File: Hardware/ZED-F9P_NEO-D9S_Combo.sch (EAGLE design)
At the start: 97 parts, among them J1 ANTENNA-SMA-GROUNDEDEDGE_SMA, J2 Qwiic Right Angle, J3 USB Female Type C Connector, J4 Qwiic Right Angle, J6 USB Female Type C Connector, U1 U-BLOX_NEO-D9S-00B, U2 3.3V, U3 POWER-DIVIDER, U4 U-BLOX_ZED-F9P

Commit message: Updates various text and symbols
* Replaces ESD Diodes and Antenna Splitter Diode with larger packages
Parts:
- removed D2, D4: PRTR5V0U2F, SparkFun-IC-Power:PRTR5V0U2F
- removed U$78: SPARKX-LOGO4, SparkX:SPARKX-LOGO4
- added LOGO2: SFE_LOGO_NAME.1_INCH, SparkFun-Aesthetics:SFE_LOGO_NAME.1_INCH
- added U5, U6: ESD Diode, SparkFun-DiscreteSemi:TVS_DIODE_ARRAY_DT1042-04SO-7
- LED1: device SparkFun-LED:LED-RED0603 -> SparkFun-LED:LED-RED_0603-KB
- R1: value 1k -> 4.7k; device SparkFun-Resistors:1KOHM-0603-1/10W-1% -> SparkFun-Resistors:4.7KOHM-0603-1/10W-1%
- U$77: value SPARKX-LOGO4 -> BP2G1+_POWER_SPLITTER; device SparkX:SPARKX-LOGO4 -> SparkFun-RF:BP2G1+_POWER_SPLITTER
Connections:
- net ANT: now also U$77.S
- net ANT_NEO: now also U$77.1
- net ANT_ZED: now also U$77.2
- net D+_NEO: now also U5.IO4; no longer D4.6
- net D+_ZED: now also U6.IO4; no longer D2.6
- net D-_NEO: now also U5.IO3; no longer D4.4
- net D-_ZED: now also U6.IO3; no longer D2.4
- net GND: now also U$77.GND, U5.VSS, U6.VSS; no longer D2.2, D4.2
- net USB_D+: now also U6.IO1; no longer D2.1
- net USB_D+1: now also U5.IO1; no longer D4.1
- net USB_D-: now also U6.IO2; no longer D2.3
- net USB_D-1: now also U5.IO2; no longer D4.3
- net V_USB: now also U6.VCC; no longer D2.5
- net V_USB_2: now also U5.VCC; no longer D4.5
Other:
- note added: "Antenna Divider - BP2G1+"
- note added: "GNSS Module: u-blox ZED-F9P"
- note added: "Iout (max): 600mA Vin (max): 6.5V Vdrop (max): 250mV Iq: 55uA"
- note added: "L-Band Corrections Module: u-blox NEO-D9S"
- note added: "L1/L2 Antenna"
- note added: "Revised By: Elias Santistevan"
- note added: "Voltage Regulation - AP2112K"
- note added: "v10"
- note removed: "AP2112K-3.3V ------------- Iout (max): 600mA Vin (max): 6.5V Vdrop (max): 250mV Iq: 55uA"
- note removed: "Antenna"
- note removed: "Antenna Divider"
- note removed: "Voltage Regulation"
- note removed: "u-blox NEO-D9S"
- note removed: "u-blox ZED-F9P"
- note removed: "x02"
- moved on the sheet: C3, I2C, R7, R8, RX2-TX2, TX2-RX2, U3

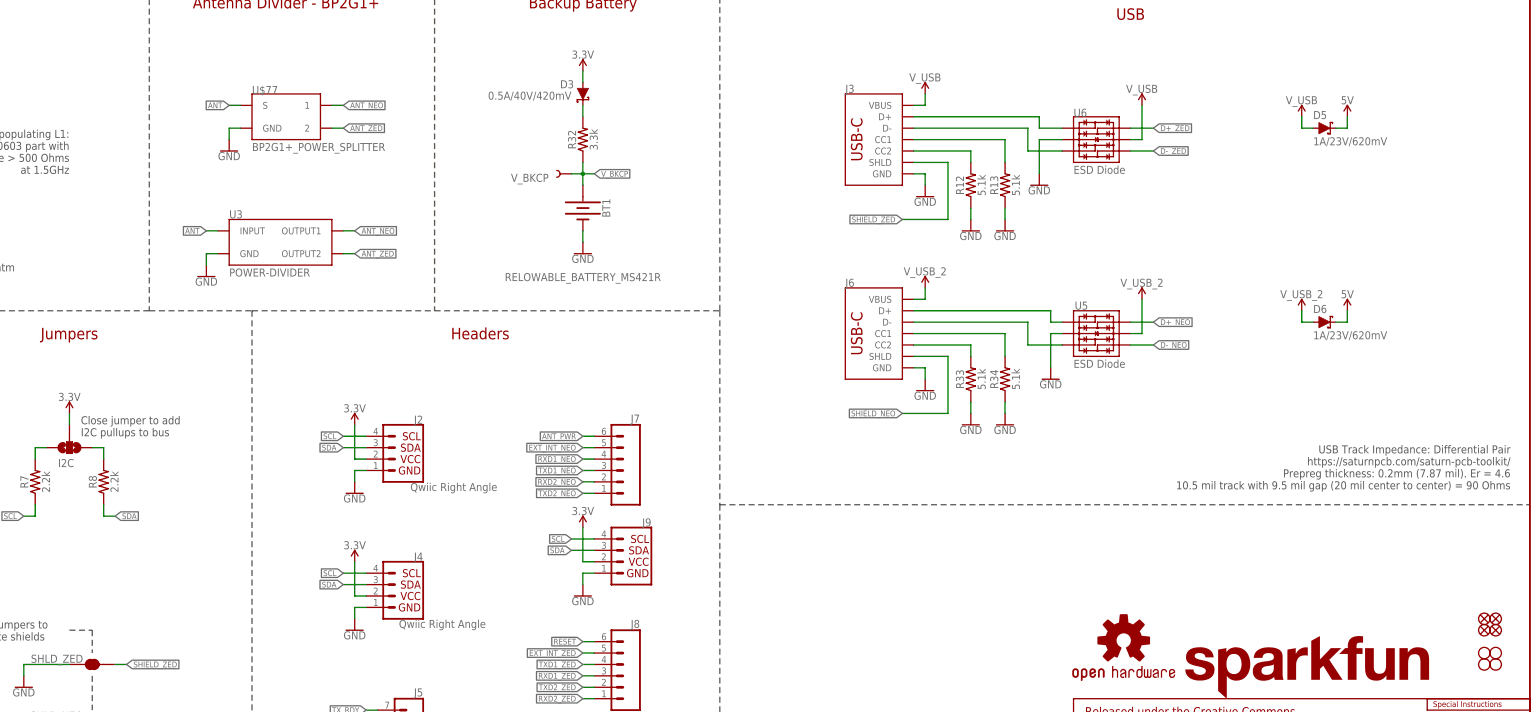
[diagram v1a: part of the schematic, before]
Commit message: Changes 90 Ohm impedance calculation to decrease trace width
* Adds additional measures
* Updates silk
* Adds polygons to USB shield
* Adds four layer numbers
* Updated ordering instructions
* Routes new antenna splitter
* Spaces out some of the more common transmission traces, UART and I2C, to minimize cross talk
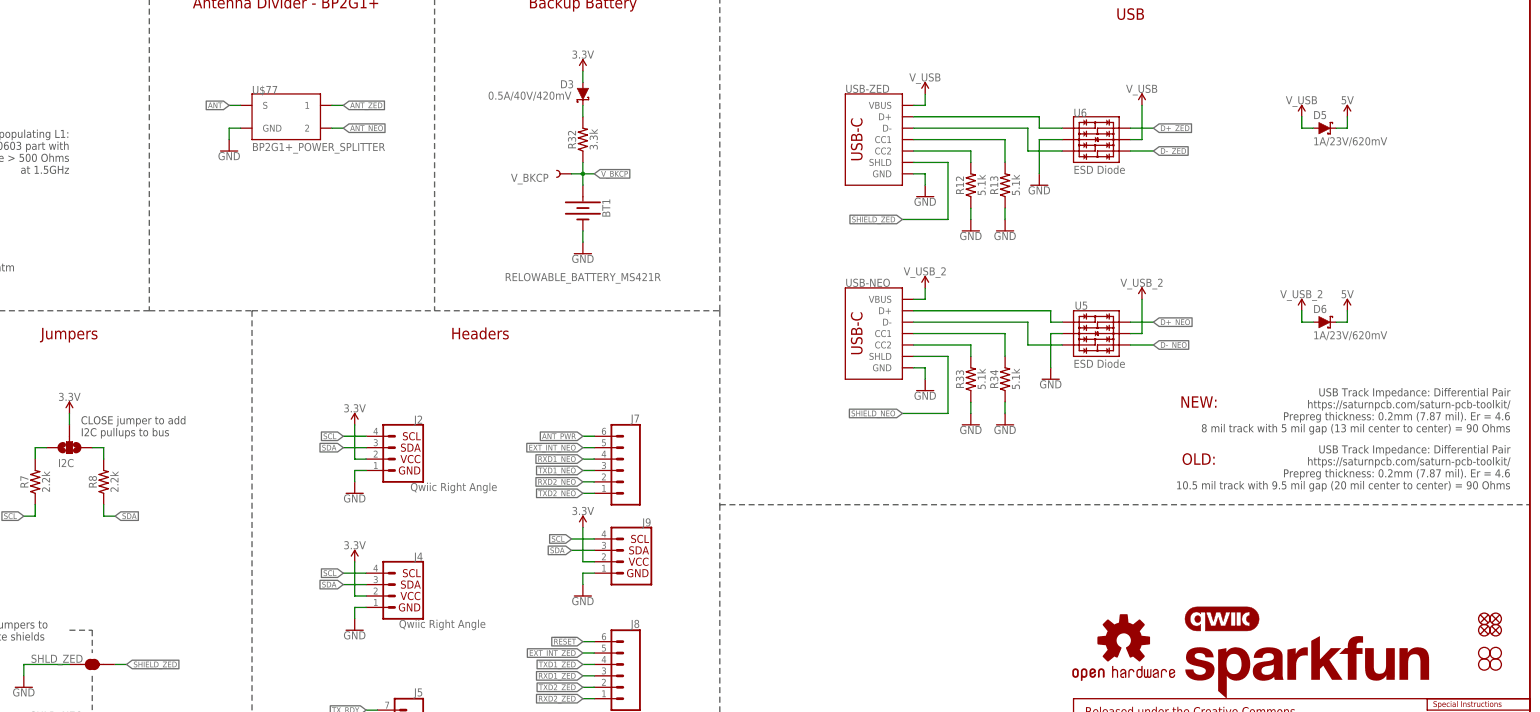
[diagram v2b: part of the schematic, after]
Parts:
- removed U3: POWER-DIVIDER, SparkFun-RF:POWER-DIVIDER
- added LOGO3: QWIIC_LOGO_5MM, SparkFun-Aesthetics:QWIIC_LOGO_5MM
- renumbered J3 to USB-ZED, J6 to USB-NEO
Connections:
- net ANT: no longer U3.INPUT
- net ANT_NEO: now also U$77.2; no longer U$77.1, U3.OUTPUT1
- net ANT_ZED: now also U$77.1; no longer U$77.2, U3.OUTPUT2
- net GND: no longer U3.GND
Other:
- note added: "CLOSE jumper to add I2C pullups to bus"
- note added: "NEW:"
- note added: "OLD:"
- note added: "USB Track Impedance: Differential Pair https://saturnpcb.com/saturn-pcb-toolkit/ Prepreg thickness: 0.2mm (7.87 mil). Er = 4.6 8 mil track with 5 mil gap (13 mil center to center) = 90 Ohms"
- note removed: "Close jumper to add I2C pullups to bus"

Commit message: Fixes ESD diode
* Adds L-Band text/silk to relevant Antenna notes
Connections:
- removed net USB_D+: U6.IO1, USB-ZED.D+
- removed net USB_D+1: U5.IO1, USB-NEO.D+
- removed net USB_D-: U6.IO2, USB-ZED.D-
- removed net USB_D-1: U5.IO2, USB-NEO.D-
- net D+_NEO: now also USB-NEO.D+
- net D+_ZED: now also USB-ZED.D+
- net D-_NEO: now also USB-NEO.D-
- net D-_ZED: now also USB-ZED.D-
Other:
- note added: "L1/L2/L-Band Antenna"
- note removed: "L1/L2 Antenna"
- note removed: "NEW:"
- note removed: "OLD:"
- note removed: "USB Track Impedance: Differential Pair https://saturnpcb.com/saturn-pcb-toolkit/ Prepreg thickness: 0.2mm (7.87 mil). Er = 4.6 10.5 mil track with 9.5 mil gap (20 mil center to center) = 90 Ohms"
- moved on the sheet: U5, U6

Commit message: Updates note for USB 90 Ohm impedance calculation
* Moves all silk out towards the PTH's
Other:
- note added: "USB Track Impedance: Differential Pair https://saturnpcb.com/saturn-pcb-toolkit/ Prepreg thickness: 0.2mm (7.1 mil). Er = 4.6 8 mil track with 5 mil gap (13 mil center to center) = 90 Ohms"
- note removed: "USB Track Impedance: Differential Pair https://saturnpcb.com/saturn-pcb-toolkit/ Prepreg thickness: 0.2mm (7.87 mil). Er = 4.6 8 mil track with 5 mil gap (13 mil center to center) = 90 Ohms"
- moved on the sheet: J1
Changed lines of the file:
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@@
 <text x="427.482" y="91.948" size="1.778" layer="97" font="vector" align="top-right">USB Track Impedance: Differential Pair
 https://saturnpcb.com/saturn-pcb-toolkit/
-Prepreg thickness: 0.2mm (7.87 mil). Er = 4.6
+Prepreg thickness: 0.2mm (7.1 mil). Er = 4.6
 8 mil track with 5 mil gap (13 mil center to center) = 90 Ohms
 </text>
@@
 <attribute name="VALUE" x="217.932" y="233.934" size="1.778" layer="96" font="vector" rot="R180" align="top-center"/>
 </instance>
-<instance part="J1" gate="G$1" x="35.56" y="175.26" smashed="yes" rot="MR0">
-<attribute name="NAME" x="40.132" y="176.53" size="1.778" layer="95" font="vector" rot="MR0"/>
+<instance part="J1" gate="G$1" x="35.56" y="177.8" smashed="yes" rot="MR0">
+<attribute name="NAME" x="40.132" y="179.07" size="1.778" layer="95" font="vector" rot="MR0"/>
 </instance>
 <instance part="J5" gate="J1" x="180.34" y="22.86" smashed="yes" rot="MR0">
@@
 </instance>
 <instance part="C7" gate="G$1" x="73.66" y="172.72" smashed="yes" rot="R90">
-<attribute name="NAME" x="70.739" y="174.244" size="1.778" layer="95" font="vector" rot="R90"/>
-<attribute name="VALUE" x="75.819" y="174.244" size="1.778" layer="96" font="vector" rot="R90"/>
+<attribute name="NAME" x="72.136" y="179.959" size="1.778" layer="95" font="vector" rot="R180"/>
+<attribute name="VALUE" x="72.136" y="177.419" size="1.778" layer="96" font="vector" rot="R180"/>
 </instance>
 <instance part="FRAME2" gate="G$1" x="0" y="0" smashed="yes"/>
@@
 <pinref part="J1" gate="G$1" pin="GND"/>
 <pinref part="GND27" gate="1" pin="GND"/>
-<wire x1="33.02" y1="172.72" x2="33.02" y2="170.18" width="0.1524" layer="91"/>
+<wire x1="33.02" y1="175.26" x2="33.02" y2="170.18" width="0.1524" layer="91"/>
 </segment>
 <segment>
@@
 <junction x="45.72" y="172.72"/>
 <pinref part="J1" gate="G$1" pin="SIGNAL"/>
+<wire x1="35.56" y1="175.26" x2="35.56" y2="172.72" width="0.1524" layer="91"/>
 <wire x1="35.56" y1="172.72" x2="45.72" y2="172.72" width="0.1524" layer="91"/>
 <pinref part="L1" gate="L1" pin="1"/>

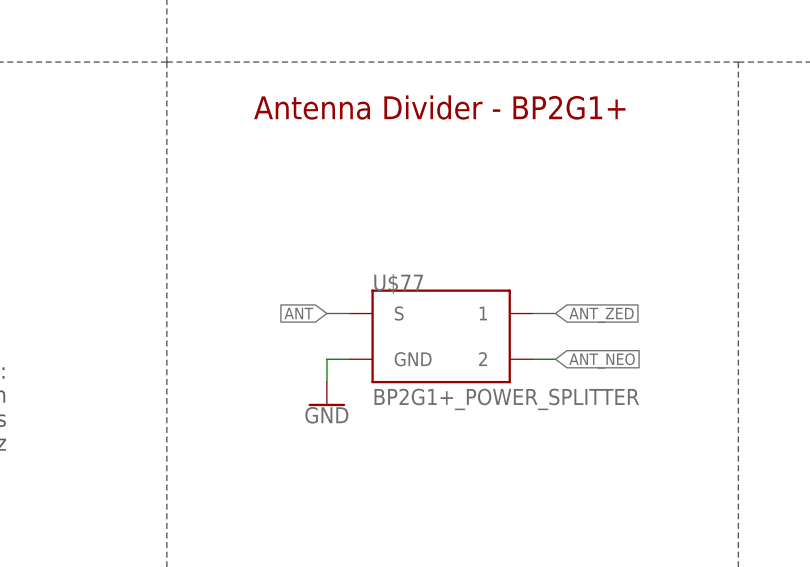
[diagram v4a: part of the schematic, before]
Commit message: Updates BP2G1+ with minor corrections
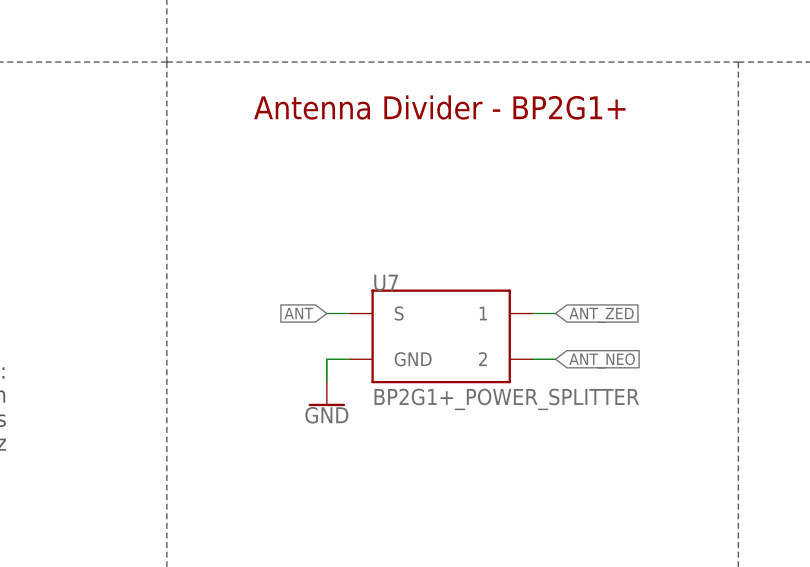
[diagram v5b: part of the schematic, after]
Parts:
- renumbered U$77 to U7
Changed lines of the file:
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@@
 <part name="U6" library="SparkFun-DiscreteSemi" deviceset="TVS_DIODE_ARRAY" device="_DT1042-04SO-7" value="ESD Diode"/>
 <part name="SUPPLY26" library="SparkFun-PowerSymbols" deviceset="V_USB_2" device=""/>
-<part name="U$77" library="SparkFun-RF" deviceset="BP2G1+_POWER_SPLITTER" device=""/>
+<part name="U7" library="SparkFun-RF" deviceset="BP2G1+_POWER_SPLITTER" device=""/>
 <part name="GND24" library="SparkFun-PowerSymbols" deviceset="GND" device=""/>
 <part name="LOGO3" library="SparkFun-Aesthetics" deviceset="QWIIC_LOGO" device="_5MM" value="QWIIC_LOGO_5MM"/>
@@
 <attribute name="VALUE" x="335.28" y="127.254" size="1.778" layer="96" font="vector" align="bottom-center"/>
 </instance>
-<instance part="U$77" gate="U1" x="154.94" y="165.1" smashed="yes">
-<attribute name="NAME" x="147.32" y="170.18" size="1.778" layer="95" font="vector"/>
-<attribute name="VALUE" x="147.32" y="157.48" size="1.778" layer="96" font="vector"/>
+<instance part="U7" gate="U1" x="154.94" y="165.1" smashed="yes">
+<attribute name="NAME" x="147.32" y="170.18" size="1.778" layer="95"/>
+<attribute name="VALUE" x="147.32" y="157.48" size="1.778" layer="96"/>
 </instance>
 <instance part="GND24" gate="1" x="142.24" y="157.48" smashed="yes">
@@
 <pinref part="GND24" gate="1" pin="GND"/>
 <wire x1="142.24" y1="162.56" x2="142.24" y2="160.02" width="0.1524" layer="91"/>
-<pinref part="U$77" gate="U1" pin="GND"/>
+<pinref part="U7" gate="U1" pin="GND"/>
 </segment>
 </net>
@@
 <wire x1="144.78" y1="167.64" x2="142.24" y2="167.64" width="0.1524" layer="91"/>
 <label x="142.24" y="167.64" size="1.27" layer="95" font="vector" rot="R180" xref="yes"/>
-<pinref part="U$77" gate="U1" pin="S"/>
+<pinref part="U7" gate="U1" pin="S"/>
 </segment>
 </net>
@@
 <wire x1="165.1" y1="162.56" x2="167.64" y2="162.56" width="0.1524" layer="91"/>
 <label x="167.64" y="162.56" size="1.27" layer="95" font="vector" xref="yes"/>
-<pinref part="U$77" gate="U1" pin="2"/>
+<pinref part="U7" gate="U1" pin="2"/>
 </segment>
 </net>
@@
 <wire x1="165.1" y1="167.64" x2="167.64" y2="167.64" width="0.1524" layer="91"/>
 <label x="167.64" y="167.64" size="1.27" layer="95" font="vector" xref="yes"/>
-<pinref part="U$77" gate="U1" pin="1"/>
-</segment>
-</net>
+<pinref part="U7" gate="U1" pin="1"/>
+</segment>
+</net>

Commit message: Replaces 1x6 PTH connector with no SKU
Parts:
- J7, J8: device SparkFun-Connectors:CONN_06NO_SILK_FEMALE_PTH -> SparkFun-Connectors:CONN_06NO_SILK_NO_POP
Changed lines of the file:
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@@
 <part name="J9" library="SparkFun-Connectors" deviceset="I2C_STANDARD" device="_NO_SILK"/>
 <part name="J10" library="SparkFun-Connectors" deviceset="I2C_STANDARD" device="_NO_SILK"/>
-<part name="J8" library="SparkFun-Connectors" deviceset="CONN_06" device="NO_SILK_FEMALE_PTH"/>
-<part name="J7" library="SparkFun-Connectors" deviceset="CONN_06" device="NO_SILK_FEMALE_PTH"/>
+<part name="J8" library="SparkFun-Connectors" deviceset="CONN_06" device="NO_SILK_NO_POP"/>
+<part name="J7" library="SparkFun-Connectors" deviceset="CONN_06" device="NO_SILK_NO_POP"/>
 <part name="V_BKCP" library="SparkFun-Connectors" deviceset="TEST-POINT" device="3X5"/>
 <part name="C10" library="SparkFun-Capacitors" deviceset="0.1UF" device="-0603-25V-(+80/-20%)" value="0.1uF"/>
